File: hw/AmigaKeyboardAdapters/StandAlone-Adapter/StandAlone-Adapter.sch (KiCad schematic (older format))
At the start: 63 parts, among them J1 RJ10, J10 Conn_01x04, J11 Conn_01x02, J2 Conn_01x03, J3 Conn_02x03_Odd_Even, J4 Conn_01x04, J5 Conn_01x05, J6 Conn_01x03, J7 Conn_01x03, J8 Conn_01x02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

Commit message: New silkscreen (back) logo
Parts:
- added LOGO4: Stalker Logo, RetroBitLab:Stalker_16.1x17.3mm, symbol AmigaComponents:LOGO

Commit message: First import for LCSC PCB Production and components placement
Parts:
- removed D2, D3: LED, LED_SMD:LED_1206_3216Metric_Pad1.42x1.75mm_HandSolder, symbol StandAlone-Adapter-rescue:LED
- removed R2, R3: 1.5K, Resistor_SMD:R_1206_3216Metric_Pad1.30x1.75mm_HandSolder, symbol StandAlone-Adapter-rescue:R
- removed USB1: USB_A, RetroBitLab:CUI_UJ2-AH-4-TH, symbol Connector:USB_A
- added USB1: USB_A_SMD_LCSC, RetroBitLab:USB_A_M04P-F000_LCSC_C386738, symbol AmigaComponents:USB_A_SMD_LCSC
- C1: value 10u -> 100nF; footprint Capacitor_Tantalum_SMD:CP_EIA-3216-12_Kemet-S_Pad1.58x1.35mm_HandSolder -> Capacitor_SMD:C_1206_3216Metric_Pad1.33x1.80mm_HandSolder; symbol StandAlone-Adapter-rescue:CP1 -> Device:C_Small; LCSC (none) -> C24497
- C10, C11, C12, C13, C14, C4, C6: LCSC (none) -> C24497
- C2: value 22u -> 10uF; symbol StandAlone-Adapter-rescue:CP1 -> Device:CP_Small; LCSC (none) -> C108529
- C3: symbol StandAlone-Adapter-rescue:C_Small -> Device:C_Small; LCSC (none) -> C24497
- C5: symbol StandAlone-Adapter-rescue:CP1_Small -> Device:CP_Small; LCSC (none) -> C108529
- C7: value 4.7u -> 4.7uF; LCSC (none) -> C7237
- C8: value 20p -> 22pF; LCSC (none) -> C1896
- C9: value 20p -> 22pF; Field4 (none) -> C1896
- D1: value LED -> RED; LCSC (none) -> C93133
- D4: value LED -> RED; symbol StandAlone-Adapter-rescue:LED -> Device:LED; LCSC (none) -> C93133
- Q1, Q2, Q3: LCSC (none) -> C489349
- R1: value 1.5K -> 330R; LCSC (none) -> C245520
- R10, R11, R12, R13, R14, R15, R6, R7, R8, R9: LCSC (none) -> C17902
- R16: value 12ohm -> 22R; symbol StandAlone-Adapter-rescue:R_Small -> Device:R_Small; LCSC (none) -> C114943
- R17: value 12ohm -> 22R; LCSC (none) -> C114943
- R4: value 22K -> 10K; LCSC (none) -> C17902
- R5: value 1.5K -> 330R; symbol StandAlone-Adapter-rescue:R -> Device:R_Small; LCSC (none) -> C245520
- RESET1: footprint RetroBitLab:SW_SPST_FSMSM_3D -> RetroBitLab:SPST-7.3x3.9x2.5-WUERTH-434121025816; LCSC (none) -> C318911
- U1: symbol StandAlone-Adapter-rescue:AZ1117-3.3 -> Regulator_Linear:LM1117-3.3; LCSC (none) -> C126027
- U2: LCSC (none) -> C74524
- XT1: footprint RetroBitLab:Crystal_HC49-4H_Vertical_3D -> Crystal:Crystal_SMD_HC49-SD; LCSC (none) -> C107426
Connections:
- net GND: now also USB1.4 (GND), USB1.~ (SH2)
- net VCC: now also USB1.1 (VBUS)
- net at R16.2: now also USB1.3 (D+)
- net at R17.2: now also USB1.2 (D-)
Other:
- note removed: "+12V PRESENT"
- note removed: "Note: Top view Pin 1 on the left. Like MODEL: UJ2-AH-4-TH from CUI INC."

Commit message: Sent to JLCPCB for quotes of 25 pcs and 100 pcs.
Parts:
- C9: Field4 C1896 -> (none); LCSC (none) -> C1896

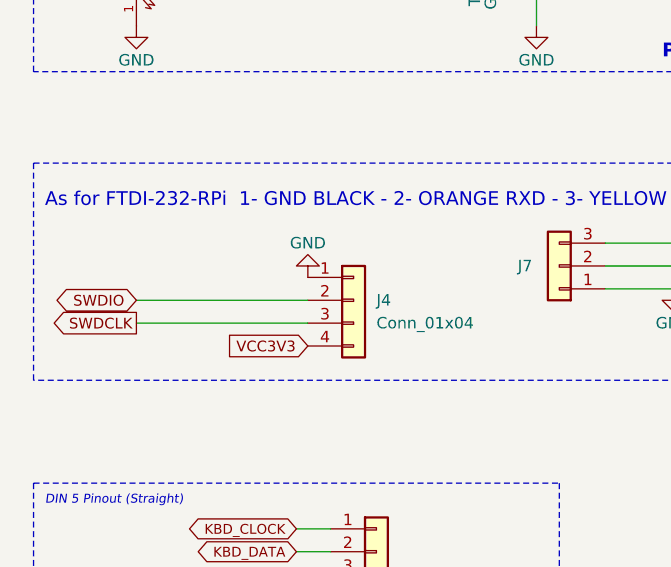
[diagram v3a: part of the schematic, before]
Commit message: Modified the JTAG STLinkV2 programmer port
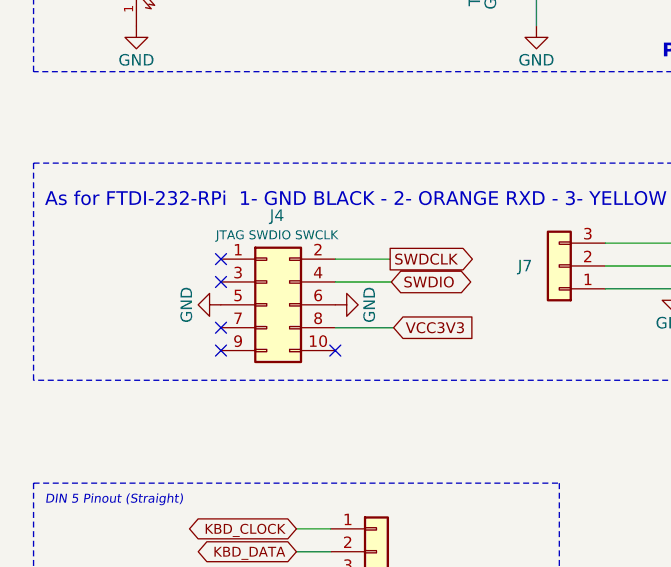
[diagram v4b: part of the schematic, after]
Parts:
- removed J4: Conn_01x04, Connector_PinHeader_2.54mm:PinHeader_1x04_P2.54mm_Horizontal, symbol Connector_Generic:Conn_01x04
- added J4: JTAG SWDIO SWCLK, Connector_IDC:IDC-Header_2x05_P2.54mm_Vertical, symbol Connector_Generic:Conn_02x05_Odd_Even
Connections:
- net GND: now also J4.5 (Pin_5), J4.6 (Pin_6)
- net SWDCLK: now also J4.2 (Pin_2)
- net SWDIO: now also J4.4 (Pin_4)
- net VCC3V3: now also J4.8 (Pin_8)
- no-connect marks 41 -> 46

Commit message: RetroBitLab library
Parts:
- LOGO1, LOGO2, LOGO3, LOGO4: symbol AmigaComponents:LOGO -> RetroBitLab:LOGO
- U2: symbol AmigaComponents:STM32F401RBTx -> RetroBitLab:STM32F401RBTx
- USB1: symbol AmigaComponents:USB_A_SMD_LCSC -> RetroBitLab:USB_A_SMD_LCSC
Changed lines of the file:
@@
 $EndComp
 $Comp
-L AmigaComponents:STM32F401RBTx U2
+L RetroBitLab:STM32F401RBTx U2
 U 1 1 60858D17
 P 8650 6100
@@
 	6500 4200 6500 4410
 $Comp
-L AmigaComponents:LOGO LOGO1
+L RetroBitLab:LOGO LOGO1
 U 1 1 6368B065
 P 6135 9240
@@
 $EndComp
 $Comp
-L AmigaComponents:LOGO LOGO2
+L RetroBitLab:LOGO LOGO2
 U 1 1 6368CBB3
 P 6570 9235
@@
 $EndComp
 $Comp
-L AmigaComponents:LOGO LOGO3
+L RetroBitLab:LOGO LOGO3
 U 1 1 63696ADE
 P 6965 9200
@@
 $EndComp
 $Comp
-L AmigaComponents:LOGO LOGO4
+L RetroBitLab:LOGO LOGO4
 U 1 1 6365EFCE
 P 7505 9145
@@
 	6550 8150 6650 8150
 $Comp
-L AmigaComponents:USB_A_SMD_LCSC USB1
+L RetroBitLab:USB_A_SMD_LCSC USB1
 U 1 1 636EB3F3
 P 14100 2450
